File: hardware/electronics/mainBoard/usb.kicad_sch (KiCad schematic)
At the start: 24 parts, among them J2 MUSBRM1C1M0, U5 TUSB4041I-Q1

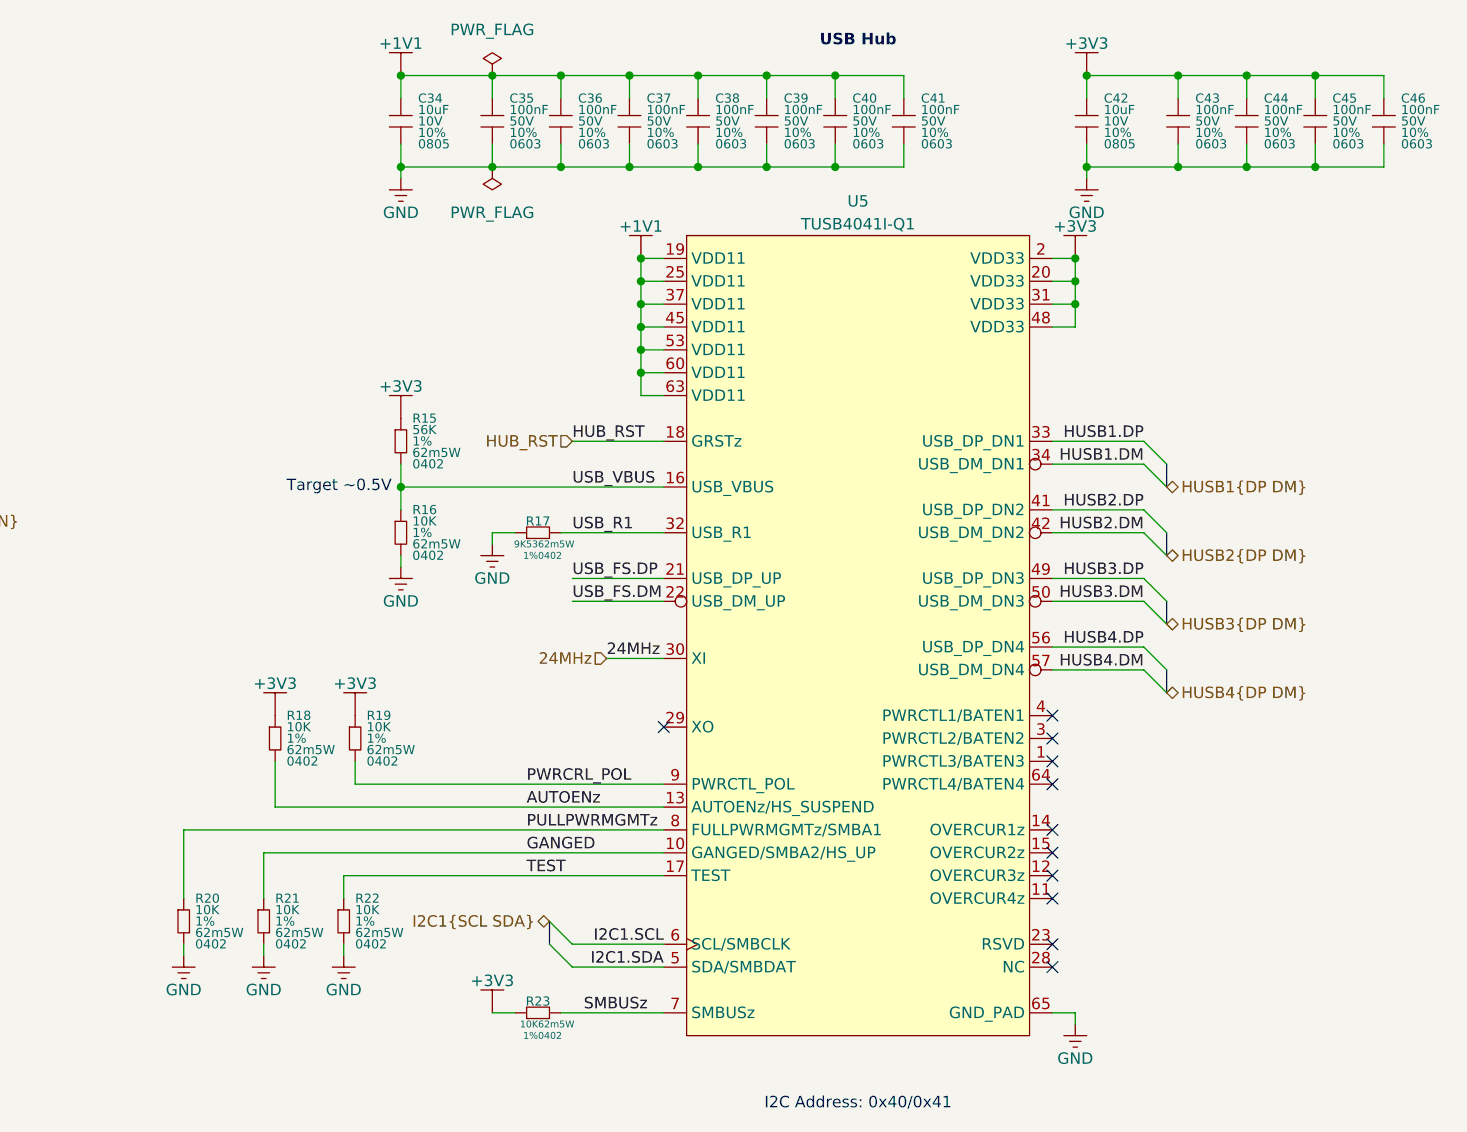
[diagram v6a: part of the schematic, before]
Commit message: removed usb hub circuitry
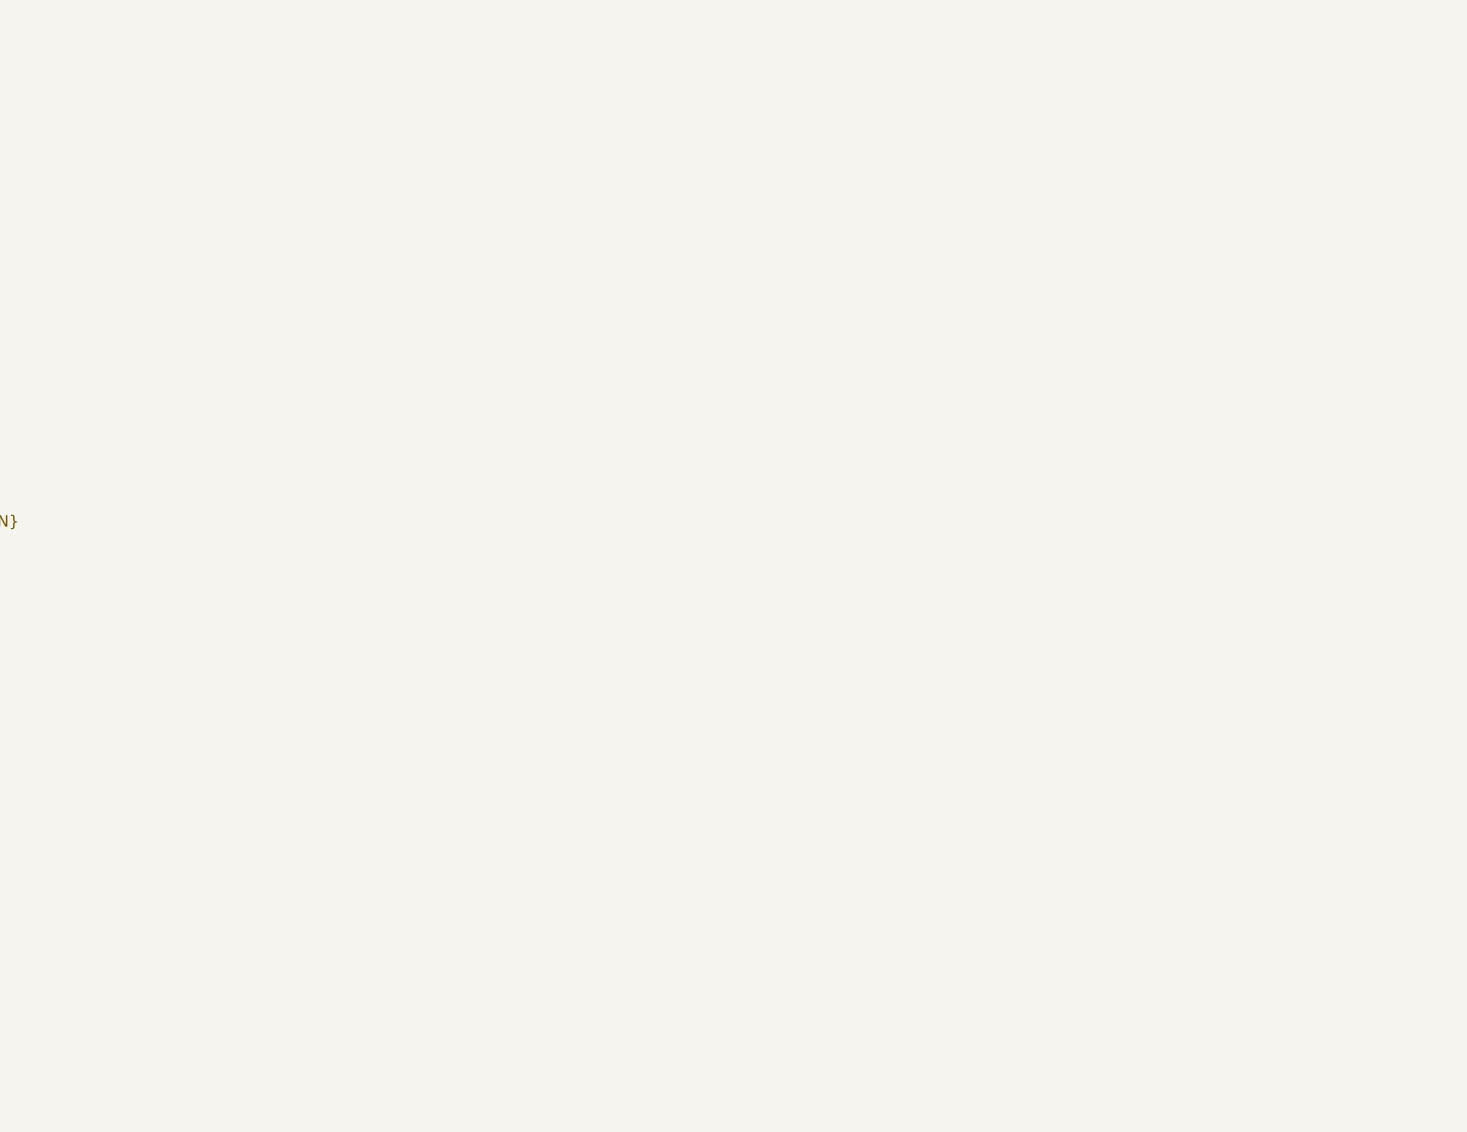
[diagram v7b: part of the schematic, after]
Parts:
- removed C34, C42: 10uF, symbol lib_sch:C
- removed C35, C36, C37, C38, C39, C40, C41, C43, C44, C45, C46: 100nF, symbol lib_sch:C
- removed R15: 56K, symbol lib_sch:R
- removed R16, R18, R19, R20, R21, R22: 10K, symbol lib_sch:R
- removed R17: 9K53, symbol lib_sch:R_horizontal
- removed R23: 10K, symbol lib_sch:R_horizontal
- removed U5: TUSB4041I-Q1, symbol lib_sch:TUSB4041I-Q1
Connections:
- no-connect marks 21 -> 10
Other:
- note removed: "I2C Address: 0x40/0x41"
- note removed: "Target ~0.5V"
- note removed: "USB Hub"
